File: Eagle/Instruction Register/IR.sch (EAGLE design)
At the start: 15 parts, among them IC1 SN74HC04N, IC2 SN74HC04N, IC3 SN74HC04N, J1 55959-1630

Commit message: Worked on IR
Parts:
- added LED12, LEDACI, LEDALUO, LEDCE, LEDCO, LEDHLT, LEDINPUT, LEDIRI, LEDIRO, LEDJMP, LEDMARI, LEDMBRI, LEDMBRO, LEDMCR, LEDOI, LEDONE, LEDRI, LEDRO, LEDSC, LEDSU: BLUE, led:LED3MM
- added R12, RACI, RALUO, RCE, RCO, RHLT, RINPUT, RIRI, RIRO, RJMP, RMARI, RMBRI, RMBRO, RMCR, ROI, RONE, RRI, RRO, RSC, RSU: 220, rcl:R-US_0204/7
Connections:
- removed net N$35: IR_OUT_0-7.!OE1, IR_OUT_0-7.!OE2, IR_OUT_8-15.!OE1, IR_OUT_8-15.!OE2
- new net !ACO: IC1.6Y
- new net !ALUO: IC1.5Y
- new net !CO: IC1.4Y
- new net !IRO: IC2.4Y, IR_OUT_0-7.!OE1, IR_OUT_0-7.!OE2, IR_OUT_8-15.!OE1, IR_OUT_8-15.!OE2
- new net !JMP: IC2.2Y
- new net !MBRO: IC2.3Y
- new net !MCR: IC1.2Y
- new net !ONE: IC1.1Y, ONE_0-7.!OE1, ONE_0-7.!OE2, ONE_8-15.!OE1, ONE_8-15.!OE2
- new net !RI: IC2.6Y
- new net !RO: IC2.5Y
- new net !RST: IC2.1Y
- new net !SC: IC1.3Y
- new net CLK: CLOCK_GATE.1A, MICROCODE_COUNTER.CLK
- new net N$10: LEDOI.A, ROI.1
- new net N$11: LEDMBRI.A, RMBRI.1
- new net N$12: LEDALUO.A, RALUO.1
- new net N$13: LEDSU.A, RSU.1
- new net N$14: LEDSC.A, RSC.1
- new net N$15: LEDCO.A, RCO.1
- new net N$16: LEDJMP.A, RJMP.1
- new net N$17: LEDRO.A, RRO.1
- new net N$19: LEDMARI.A, RMARI.1
- new net N$20: LEDMBRO.A, RMBRO.1
- new net N$21: LED12.A, R12.1
- new net N$22: LEDACI.A, RACI.1
- new net N$23: LEDCE.A, RCE.1
- new net N$24: LEDHLT.A, RHLT.1
- new net N$33: CLOCK_GATE.1Y, IR_0-7.CLK, IR_8-15.CLK
- new net N$5: LEDINPUT.A, RINPUT.1
- new net N$6: LEDONE.A, RONE.1
- new net N$7: LEDMCR.A, RMCR.1
- new net N$8: LEDIRI.A, RIRI.1
- new net N$9: LEDIRO.A, RIRO.1
- new net RST: IC2.1A
- net ACI: now also RACI.2
- net ACO: now also IC1.6A, R12.2
- net ALUO: now also IC1.5A, RALUO.2
- net CE: now also RCE.2
- net CO: now also IC1.4A, RCO.2
- net GND: now also IC1.GND, IC2.GND, LED12.C, LEDACI.C, LEDALUO.C, LEDCE.C, LEDCO.C, LEDHLT.C, LEDINPUT.C, LEDIRI.C, LEDIRO.C, LEDJMP.C, LEDMARI.C, LEDMBRI.C, LEDMBRO.C, LEDMCR.C, LEDOI.C, LEDONE.C, LEDRI.C, LEDRO.C, LEDSC.C, LEDSU.C
- net HLT: now also RHLT.2
- net INPUT: now also RINPUT.2
- net IRI: now also CLOCK_GATE.1B, RIRI.2
- net IRO: now also IC2.4A, RIRO.2
- net JMP: now also IC2.2A, RJMP.2
- net MARI: now also RMARI.2
- net MBRI: now also RMBRI.2
- net MBRO: now also IC2.3A, RMBRO.2
- net MCR: now also IC1.2A, RMCR.2
- net N$18: now also LEDRI.A, RRI.1; no longer ONE_0-7.!OE1, ONE_0-7.!OE2, ONE_8-15.!OE1, ONE_8-15.!OE2
- net OI: now also ROI.2
- net ONE: now also IC1.1A, RONE.2
- net RI: now also IC2.6A, RRI.2
- net RO: now also IC2.5A, RRO.2
- net SC: now also IC1.3A, RSC.2
- net SU: now also RSU.2
- net VCC: now also IC1.VCC, IC2.VCC

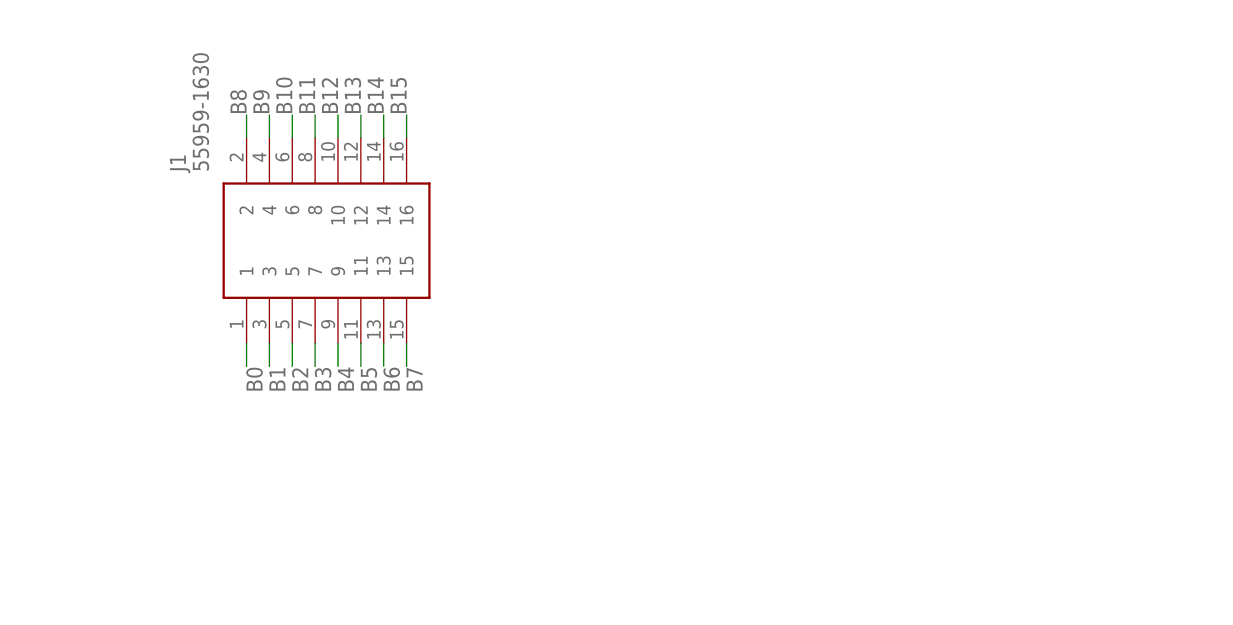
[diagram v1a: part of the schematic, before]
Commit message: added parts needed to finish boards
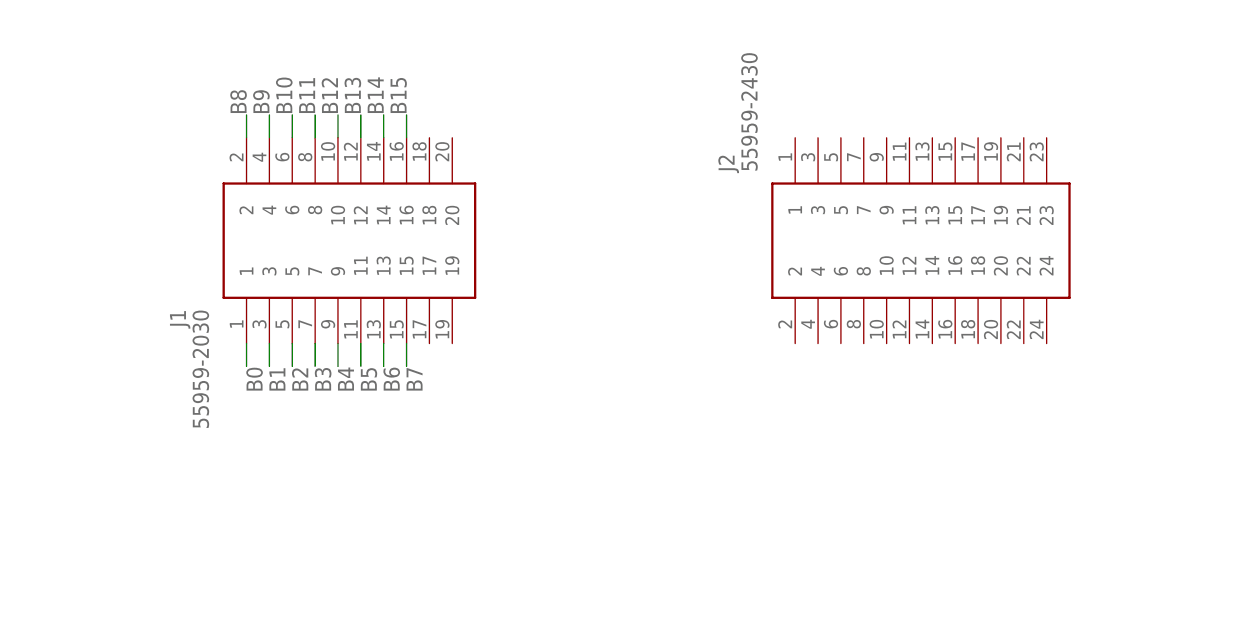
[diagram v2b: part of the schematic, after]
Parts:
- added J2: 55959-2430, SamacSys_Parts:55959-2430
- J1: value 55959-1630 -> 55959-2030; device SamacSys_Parts:55959-1630 -> SamacSys_Parts:55959-2030
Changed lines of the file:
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@@
 <part name="ONE_0-7" library="SamacSys_Parts" deviceset="SN74HC541N" device=""/>
 <part name="ONE_8-15" library="SamacSys_Parts" deviceset="SN74HC541N" device=""/>
-<part name="J1" library="SamacSys_Parts" deviceset="55959-1630" device=""/>
 <part name="IC1" library="SamacSys_Parts" deviceset="SN74HC04N" device=""/>
 <part name="IC2" library="SamacSys_Parts" deviceset="SN74HC04N" device=""/>
@@
 <part name="RHLT" library="rcl" library_urn="urn:adsk.eagle:library:334" deviceset="R-US_" device="0204/7" package3d_urn="urn:adsk.eagle:package:23498/2" value="220"/>
 <part name="LEDHLT" library="led" library_urn="urn:adsk.eagle:library:259" deviceset="LED" device="3MM" package3d_urn="urn:adsk.eagle:package:15797/1" value="BLUE"/>
+<part name="J1" library="SamacSys_Parts" deviceset="55959-2030" device=""/>
+<part name="J2" library="SamacSys_Parts" deviceset="55959-2430" device=""/>
 </parts>
 <sheets>
@@
 <attribute name="VALUE" x="237.49" y="99.06" size="1.778" layer="96" align="center-left"/>
 </instance>
-<instance part="J1" gate="G$1" x="-43.18" y="157.48" smashed="yes" rot="R90">
-<attribute name="NAME" x="-50.8" y="176.53" size="1.778" layer="95" rot="R90" align="center-left"/>
-<attribute name="VALUE" x="-48.26" y="176.53" size="1.778" layer="96" rot="R90" align="center-left"/>
-</instance>
 <instance part="IC1" gate="G$1" x="15.24" y="17.78" smashed="yes">
 <attribute name="NAME" x="36.83" y="25.4" size="1.778" layer="95" align="center-left"/>
@@
 <attribute name="NAME" x="303.276" y="-88.392" size="1.778" layer="95" rot="R90"/>
 <attribute name="VALUE" x="305.435" y="-88.392" size="1.778" layer="96" rot="R90"/>
+</instance>
+<instance part="J1" gate="G$1" x="-43.18" y="180.34" smashed="yes" rot="MR270">
+<attribute name="NAME" x="-50.8" y="161.29" size="1.778" layer="95" rot="MR270" align="center-left"/>
+<attribute name="VALUE" x="-48.26" y="161.29" size="1.778" layer="96" rot="MR270" align="center-left"/>
+</instance>
+<instance part="J2" gate="G$1" x="17.78" y="157.48" smashed="yes" rot="R90">
+<attribute name="NAME" x="10.16" y="176.53" size="1.778" layer="95" rot="R90" align="center-left"/>
+<attribute name="VALUE" x="12.7" y="176.53" size="1.778" layer="96" rot="R90" align="center-left"/>
 </instance>
 </instances>
@@
 </segment>
 <segment>
-<pinref part="J1" gate="G$1" pin="1"/>
 <wire x1="-43.18" y1="157.48" x2="-43.18" y2="154.94" width="0.1524" layer="91"/>
 <label x="-43.18" y="154.94" size="1.778" layer="95" rot="R270"/>
+<pinref part="J1" gate="G$1" pin="1"/>
 </segment>
 <segment>
@@
 <net name="B1" class="0">
 <segment>
-<pinref part="J1" gate="G$1" pin="3"/>
 <wire x1="-40.64" y1="157.48" x2="-40.64" y2="154.94" width="0.1524" layer="91"/>
 <label x="-40.64" y="154.94" size="1.778" layer="95" rot="R270"/>
+<pinref part="J1" gate="G$1" pin="3"/>
 </segment>
 <segment>
@@
 <net name="B2" class="0">
 <segment>
-<pinref part="J1" gate="G$1" pin="5"/>
 <wire x1="-38.1" y1="157.48" x2="-38.1" y2="154.94" width="0.1524" layer="91"/>
 <label x="-38.1" y="154.94" size="1.778" layer="95" rot="R270"/>
+<pinref part="J1" gate="G$1" pin="5"/>
 </segment>
 <segment>
@@
 <net name="B3" class="0">
 <segment>
-<pinref part="J1" gate="G$1" pin="7"/>
 <wire x1="-35.56" y1="157.48" x2="-35.56" y2="154.94" width="0.1524" layer="91"/>
 <label x="-35.56" y="154.94" size="1.778" layer="95" rot="R270"/>
+<pinref part="J1" gate="G$1" pin="7"/>
 </segment>
 <segment>
@@
 <net name="B4" class="0">
 <segment>
-<pinref part="J1" gate="G$1" pin="9"/>
 <wire x1="-33.02" y1="157.48" x2="-33.02" y2="154.94" width="0.1524" layer="91"/>
 <label x="-33.02" y="154.94" size="1.778" layer="95" rot="R270"/>
+<pinref part="J1" gate="G$1" pin="9"/>
 </segment>
 <segment>
@@
 <net name="B5" class="0">
 <segment>
-<pinref part="J1" gate="G$1" pin="11"/>
 <wire x1="-30.48" y1="157.48" x2="-30.48" y2="154.94" width="0.1524" layer="91"/>
 <label x="-30.48" y="154.94" size="1.778" layer="95" rot="R270"/>
+<pinref part="J1" gate="G$1" pin="11"/>
 </segment>
 <segment>
@@
 <net name="B6" class="0">
 <segment>
-<pinref part="J1" gate="G$1" pin="13"/>
 <wire x1="-27.94" y1="157.48" x2="-27.94" y2="154.94" width="0.1524" layer="91"/>
 <label x="-27.94" y="154.94" size="1.778" layer="95" rot="R270"/>
+<pinref part="J1" gate="G$1" pin="13"/>
 </segment>
 <segment>
@@
 <net name="B7" class="0">
 <segment>
-<pinref part="J1" gate="G$1" pin="15"/>
 <wire x1="-25.4" y1="157.48" x2="-25.4" y2="154.94" width="0.1524" layer="91"/>
 <label x="-25.4" y="154.94" size="1.778" layer="95" rot="R270"/>
+<pinref part="J1" gate="G$1" pin="15"/>
 </segment>
 <segment>
@@
 <net name="B15" class="0">
 <segment>
-<pinref part="J1" gate="G$1" pin="16"/>
 <wire x1="-25.4" y1="180.34" x2="-25.4" y2="182.88" width="0.1524" layer="91"/>
 <label x="-25.4" y="182.88" size="1.778" layer="95" rot="R90"/>
+<pinref part="J1" gate="G$1" pin="16"/>
 </segment>
 <segment>
@@
 <net name="B14" class="0">
 <segment>
-<pinref part="J1" gate="G$1" pin="14"/>
 <wire x1="-27.94" y1="180.34" x2="-27.94" y2="182.88" width="0.1524" layer="91"/>
 <label x="-27.94" y="182.88" size="1.778" layer="95" rot="R90"/>
+<pinref part="J1" gate="G$1" pin="14"/>
 </segment>
 <segment>
@@
 <net name="B13" class="0">
 <segment>
-<pinref part="J1" gate="G$1" pin="12"/>
 <wire x1="-30.48" y1="180.34" x2="-30.48" y2="182.88" width="0.1524" layer="91"/>
 <label x="-30.48" y="182.88" size="1.778" layer="95" rot="R90"/>
+<pinref part="J1" gate="G$1" pin="12"/>
 </segment>
 <segment>
@@
 <net name="B12" class="0">
 <segment>
-<pinref part="J1" gate="G$1" pin="10"/>
 <wire x1="-33.02" y1="180.34" x2="-33.02" y2="182.88" width="0.1524" layer="91"/>
 <label x="-33.02" y="182.88" size="1.778" layer="95" rot="R90"/>
+<pinref part="J1" gate="G$1" pin="10"/>
 </segment>
 <segment>
@@
 <net name="B11" class="0">
 <segment>
-<pinref part="J1" gate="G$1" pin="8"/>
 <wire x1="-35.56" y1="180.34" x2="-35.56" y2="182.88" width="0.1524" layer="91"/>
 <label x="-35.56" y="182.88" size="1.778" layer="95" rot="R90"/>
+<pinref part="J1" gate="G$1" pin="8"/>
 </segment>
 <segment>
@@
 <net name="B10" class="0">
 <segment>
-<pinref part="J1" gate="G$1" pin="6"/>
 <wire x1="-38.1" y1="180.34" x2="-38.1" y2="182.88" width="0.1524" layer="91"/>
 <label x="-38.1" y="182.88" size="1.778" layer="95" rot="R90"/>
+<pinref part="J1" gate="G$1" pin="6"/>
 </segment>
 <segment>
@@
 <net name="B9" class="0">
 <segment>
-<pinref part="J1" gate="G$1" pin="4"/>
 <wire x1="-40.64" y1="180.34" x2="-40.64" y2="182.88" width="0.1524" layer="91"/>
 <label x="-40.64" y="182.88" size="1.778" layer="95" rot="R90"/>
+<pinref part="J1" gate="G$1" pin="4"/>
 </segment>
 <segment>
@@
 <net name="B8" class="0">
 <segment>
-<pinref part="J1" gate="G$1" pin="2"/>
 <wire x1="-43.18" y1="180.34" x2="-43.18" y2="182.88" width="0.1524" layer="91"/>
 <label x="-43.18" y="182.88" size="1.778" layer="95" rot="R90"/>
-</segment>
-<segment>
+<pinref part="J1" gate="G$1" pin="2"/>
+</segment>
+<segment>

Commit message: Finished IR
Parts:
- removed IC3: SN74HC04N, SamacSys_Parts:SN74HC04N
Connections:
- removed net N$25: CONTROL_LOGIC_0-7.I/O0
- removed net N$26: CONTROL_LOGIC_0-7.I/O1
- removed net N$27: CONTROL_LOGIC_0-7.I/O2
- removed net N$28: CONTROL_LOGIC_0-7.I/O3
- new net C0: CONTROL_LOGIC_0-7.I/O0, J2.1
- new net C1: CONTROL_LOGIC_0-7.I/O1, J2.3
- new net C2: CONTROL_LOGIC_0-7.I/O2, J2.5
- new net C3: CONTROL_LOGIC_0-7.I/O3, J2.7
- net !ACO: now also J2.11
- net !ALUO: now also J2.15
- net !CO: now also J2.19
- net !IRO: now also J2.14
- net !JMP: now also J2.23
- net !MBRO: now also J2.4
- net !MCR: now also J2.20, MICROCODE_COUNTER.!CLR
- net !ONE: now also J2.12
- net !RI: now also J2.8
- net !RO: now also J2.10
- net !SC: now also J2.9
- net ACI: now also J2.13
- net CE: now also J2.21
- net CLK: now also J1.18
- net GND: now also CLOCK_GATE.2A, CLOCK_GATE.2B, CLOCK_GATE.3A, CLOCK_GATE.3B, CLOCK_GATE.4A, CLOCK_GATE.4B, J1.20
- net HLT: now also J2.24
- net INPUT: now also J2.18
- net IRI: now also J2.16
- net MARI: now also J2.6
- net MBRI: now also J2.2
- net OI: now also J2.22
- net RST: now also J1.17
- net SU: now also J2.17
- net VCC: now also J1.19

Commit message: finished most boards
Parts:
- added C1, C2, C3, C4: (no value), rcl:C-US025-024X044
- added LED0, LED1, LED10, LED11, LED2, LED3, LED4, LED5, LED6, LED7, LED8, LED9: YELLOW, led:LED3MM
- added LED13, LED14, LED15, LEDACO: BLUE, led:LED3MM
- added R0, R1, R10, R11, R13, R14, R15, R2, R3, R4, R5, R6, R7, R8, R9, RACO: 220, rcl:R-US_0204/7
- renumbered IC1 to NOT_GATE_1, IC2 to NOT_GATE_2, J1 to BUS, J2 to CONTROL_LOGIC
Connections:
- new net N$21: LEDACO.A, RACO.1
- new net N$25: LED1.A, R1.1
- new net N$26: LED2.A, R2.1
- new net N$27: LED3.A, R3.1
- new net N$28: LED4.A, R4.1
- new net N$29: LED5.A, R5.1
- new net N$30: LED6.A, R6.1
- new net N$31: LED7.A, R7.1
- new net N$32: LED8.A, R8.1
- new net N$34: LED9.A, R9.1
- new net N$35: LED10.A, R10.1
- new net N$36: LED11.A, R11.1
- new net N$38: LED13.A, R13.1
- new net N$39: LED14.A, R14.1
- new net N$40: LED15.A, R15.1
- new net N$41: LED0.A, R0.1
- new net N$42: LED0.C, LED1.C, LED10.C, LED11.C, LED12.C, LED13.C, LED14.C, LED15.C, LED2.C, LED3.C, LED4.C, LED5.C, LED6.C, LED7.C, LED8.C, LED9.C
- net ACO: now also RACO.2; no longer R12.2
- net GND: now also C1.1, C2.1, C3.1, C4.1, LEDACO.C; no longer LED12.C
- net IR0: now also R0.2
- net IR1: now also R1.2
- net IR10: now also R10.2
- net IR11: now also R11.2
- net IR12: now also R12.2
- net IR13: now also R13.2
- net IR14: now also R14.2
- net IR15: now also R15.2
- net IR2: now also R2.2
- net IR3: now also R3.2
- net IR4: now also R4.2
- net IR5: now also R5.2
- net IR6: now also R6.2
- net IR7: now also R7.2
- net IR8: now also R8.2
- net IR9: now also R9.2
- net VCC: now also C1.2, C2.2, C3.2, C4.2
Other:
- moved on the sheet: LED12, R12

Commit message: added Clock
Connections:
- new net !CLK: BUS.17, MICROCODE_COUNTER.CLK
- net CLK: no longer MICROCODE_COUNTER.CLK
- net RST: no longer BUS.17

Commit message: added gerber files for ordering boards
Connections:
- removed net !RST: NOT_GATE_2.1Y
- removed net RST: NOT_GATE_2.1A
- net VCC: now also NOT_GATE_2.1A
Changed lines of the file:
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@@
 <label x="261.62" y="7.62" size="1.778" layer="95" rot="R90"/>
+</segment>
+<segment>
+<pinref part="NOT_GATE_2" gate="G$1" pin="1A"/>
+<wire x1="15.24" y1="-12.7" x2="12.7" y2="-12.7" width="0.1524" layer="91"/>
+<label x="12.7" y="-12.7" size="1.778" layer="95" rot="R180"/>
 </segment>
 </net>
@@
 </segment>
 </net>
-<net name="RST" class="0">
-<segment>
-<pinref part="NOT_GATE_2" gate="G$1" pin="1A"/>
-<wire x1="15.24" y1="-12.7" x2="12.7" y2="-12.7" width="0.1524" layer="91"/>
-<label x="12.7" y="-12.7" size="1.778" layer="95" rot="R180"/>
-</segment>
-</net>
-<net name="!RST" class="0">
-<segment>
-<pinref part="NOT_GATE_2" gate="G$1" pin="1Y"/>
-<wire x1="15.24" y1="-15.24" x2="12.7" y2="-15.24" width="0.1524" layer="91"/>
-<label x="12.7" y="-15.24" size="1.778" layer="95" rot="R180"/>
-</segment>
-</net>
